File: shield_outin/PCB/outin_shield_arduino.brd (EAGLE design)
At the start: 68.6 x 53.3 mm, 27 parts, among them SW1 POWER, SW2 I2C_PWR, SW3 SERIAL_PWR, SW4 SWITCH-TACT-6MM

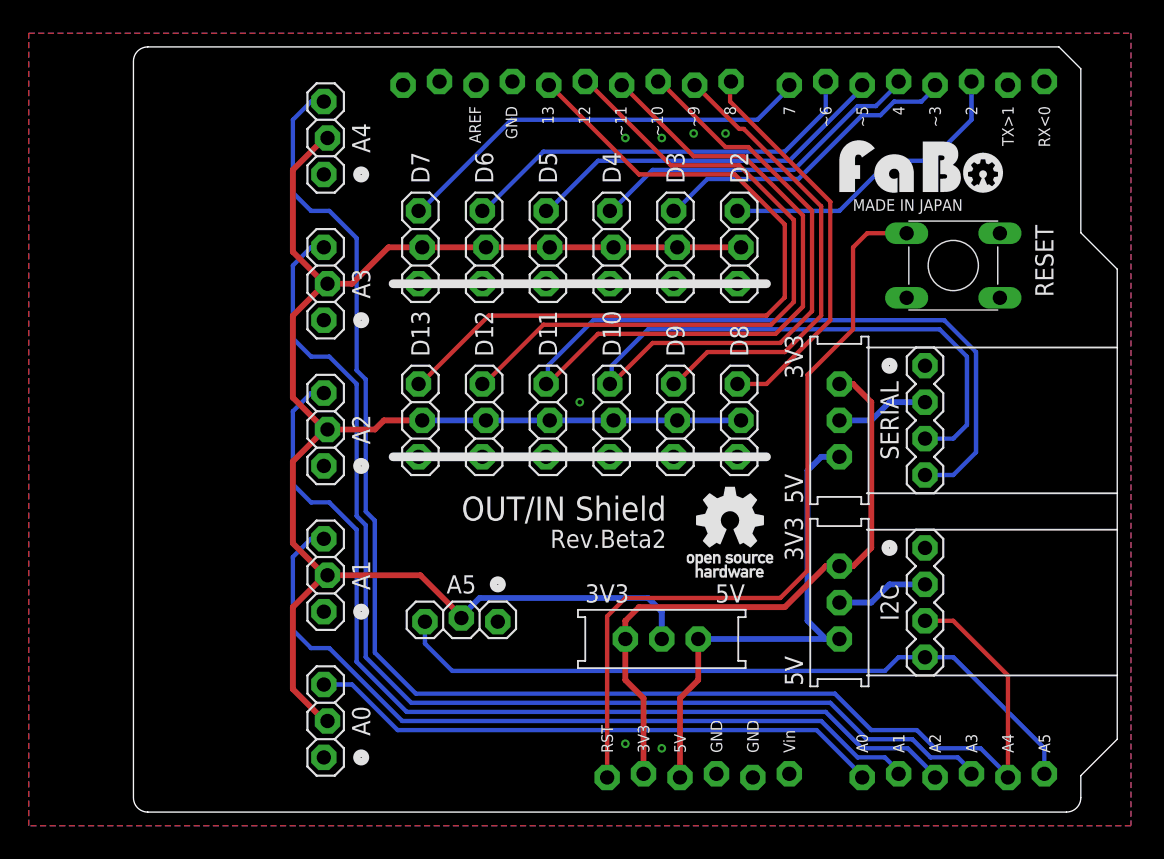
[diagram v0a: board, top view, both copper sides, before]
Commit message: change serial vcc level convert  outin_shield_arduino
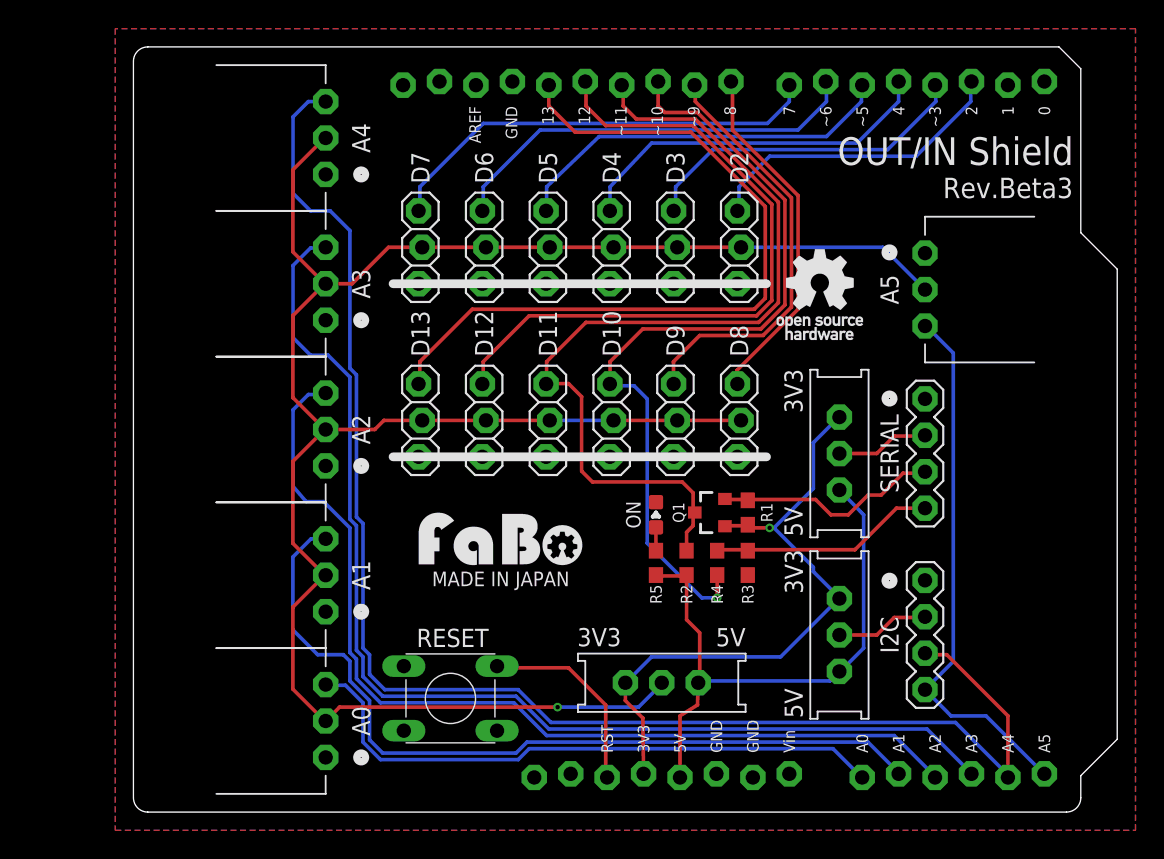
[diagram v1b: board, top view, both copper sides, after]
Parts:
- added ON: (no value), Gclue:EIA0603-LED
- added Q1: (no value), Gclue:SOT23-3
- added R1, R2, R3, R4, R5: (no value), Gclue:EIA0603
- A0, A1, A2, A3, A4, A5: device Gclue:1X3-SNEAKY -> Gclue:BRICK_3PIN_CONNECTOR
- SW4: value SWITCH-TACT-6MM -> RESET
- moved SW4 46.3 mm to (22.1, 7.92)
- moved A5 39.7 mm to (55.2, 36.4), turned to 270 degrees
- moved U$5 39.2 mm to (25.6, 17.2)
- moved U$4 17.7 mm to (47.9, 36.9)
- moved SW1 3.05 mm to (36.8, 9.02)
- moved SV2 2.31 mm to (55.2, 25.0)
- moved SW3 2.31 mm to (49.2, 25.0)
- moved SV1 2.26 mm to (55.2, 12.3)
- moved SW2 2.26 mm to (49.2, 12.3)
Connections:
- removed net RESET: SW4.4, U1.RESET
- new net N$2: SW4.3, U1.RESET
- new net N$4: ON.A, R5.2
- new net RX: R3.2, R4.1, SV2.RX
- new net TX: Q1.2, R1.1, SV2.TX
- net 3V3: now also Q1.1, R1.2
- net 5V: now also R2.2, R5.1
- net GND: now also A0.GND, A1.GND, A2.GND, A3.GND, A4.GND, A5.GND, ON.C, R3.1, SW4.2; no longer A0.1, A1.1, A2.1, A3.1, A4.1, A5.1, SW4.1
- net OUT10: now also R4.2; no longer SV2.RX
- net OUT11: now also Q1.3, R2.1; no longer SV2.TX
- net SEN0: now also A0.IN/OUT; no longer A0.3
- net SEN1: now also A1.IN/OUT; no longer A1.3
- net SEN2: now also A2.IN/OUT; no longer A2.3
- net SEN3: now also A3.IN/OUT; no longer A3.3
- net SEN4: now also A4.IN/OUT; no longer A4.3
- net SEN5: now also A5.IN/OUT; no longer A5.3
- net VCC: now also A0.VCC, A1.VCC, A2.VCC, A3.VCC, A4.VCC, A5.VCC; no longer A0.2, A1.2, A2.2, A3.2, A4.2, A5.2
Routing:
- net RESET: track 54.5 -> 0.00 mm
- net OUT11: track 87.5 -> 62.2 mm
- net OUT10: track 73.6 -> 57.1 mm, vias 0 -> 1
- net RX: track 0.00 -> 15.8 mm
- net TX: track 0.00 -> 15.7 mm
- net N$2: track 0.00 -> 13.8 mm
- net SEN5: track 50.3 -> 37.8 mm
- net VCC: track 135.5 -> 146.2 mm, vias 0 -> 1
- net 5V: track 34.9 -> 41.7 mm
- net SEN1: track 54.3 -> 57.4 mm
- net OUT8: track 27.9 -> 24.8 mm
- net OUT9: track 32.2 -> 29.6 mm
- net SEN0: track 40.3 -> 42.3 mm
- net OUT4: track 23.9 -> 25.7 mm
- net N$4: track 0.00 -> 1.63 mm
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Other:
- board text added: "0"
- board text added: "1"
- board text added: "Rev.Beta3"
- board text removed: "RX<0"
- board text removed: "Rev.Beta2"
- board text removed: "TX>1"

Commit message: change layout outin_shield_arduino
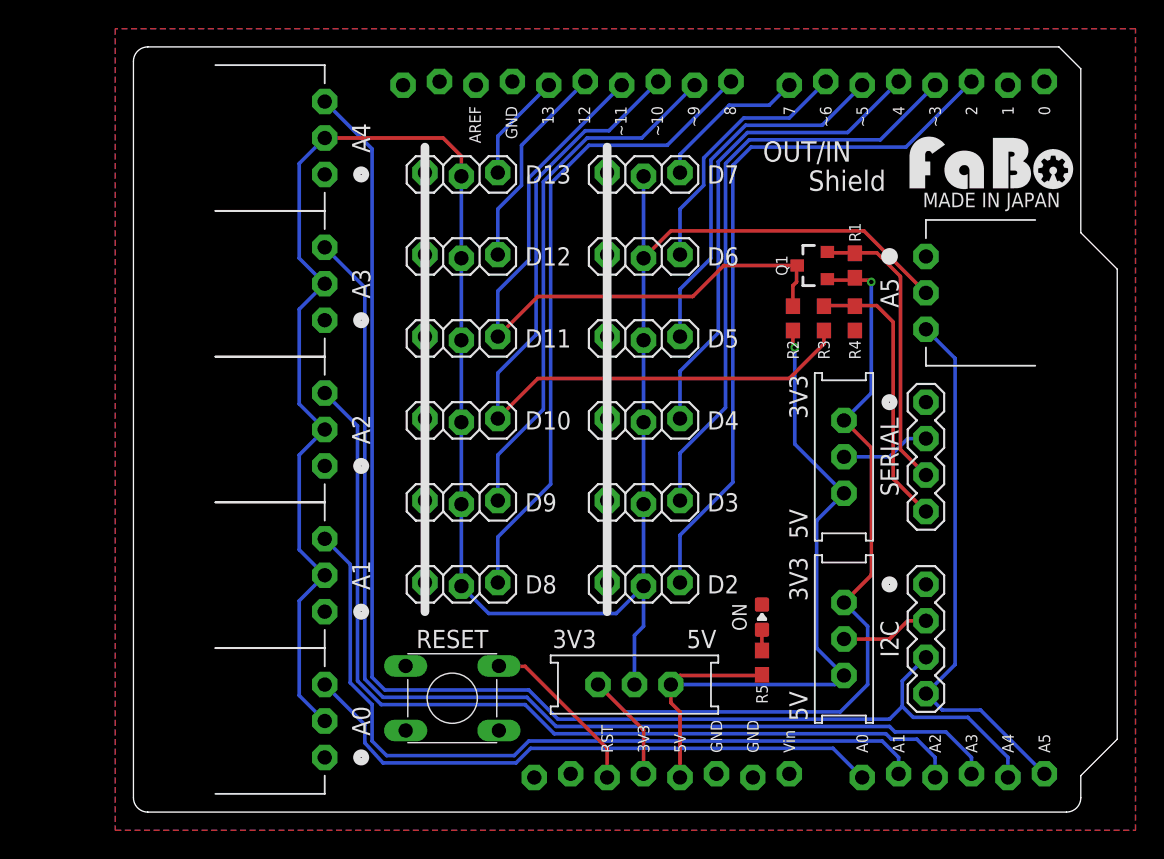
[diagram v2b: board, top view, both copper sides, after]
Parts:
- removed U$4: (no value), Gclue:LOGO_OSHW_T_M
- added U$2: (no value), Gclue:LOGO_OSHW_T_M_BOTTOM
- OUT10, OUT11, OUT12, OUT13, OUT2, OUT3, OUT4, OUT5, OUT6, OUT7, OUT8, OUT9: device Gclue:1X3-SNEAKY -> Gclue:1X3-SNEAKY-BRICK
- moved U$5 43.1 mm to (59.8, 43.4)
- moved OUT2 24.4 mm to (35.6, 15.9), turned to 0 degrees
- moved OUT8 22.5 mm to (22.9, 15.9), turned to 0 degrees
- moved R4 19.6 mm to (50.3, 34.4), turned to 90 degrees
- moved R1 18.8 mm to (50.3, 38.1)
- moved Q1 18.6 mm to (47.4, 38.1)
- moved R2 18.6 mm to (46.0, 34.4)
- moved OUT3 17.9 mm to (35.6, 21.6), turned to 0 degrees
- moved R3 17.9 mm to (48.1, 34.4), turned to 270 degrees
- moved OUT13 17.4 mm to (22.9, 44.5), turned to 0 degrees
- moved OUT7 16.4 mm to (35.6, 44.5), turned to 0 degrees
- moved OUT9 16.0 mm to (22.9, 21.6), turned to 0 degrees
- moved OUT4 12.3 mm to (35.6, 27.3), turned to 0 degrees
- moved OUT12 11.5 mm to (22.9, 38.7), turned to 0 degrees
- moved OUT6 11.1 mm to (35.6, 38.7), turned to 0 degrees
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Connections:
- net GND: now also R4.1; no longer R3.1
- net OUT10: now also R3.2; no longer R4.2
- net RX: now also R3.1, R4.2; no longer R3.2, R4.1
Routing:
- net OUT13: track 53.3 -> 7.57 mm
- net OUT12: track 47.7 -> 14.6 mm
- net OUT2: track 21.7 -> 49.7 mm
- net OUT7: track 31.1 -> 10.9 mm
- net OUT8: track 24.8 -> 44.9 mm
- net 3V3: track 44.3 -> 62.5 mm
- net OUT3: track 23.5 -> 41.7 mm
- net OUT11: track 62.2 -> 47.0 mm
- net VCC: track 146.2 -> 158.8 mm, vias 1 -> 0
- net OUT6: track 29.5 -> 18.1 mm
- net 5V: track 41.7 -> 52.8 mm, vias 0 -> 1
- net SEN4: track 104.1 -> 94.4 mm
- net OUT4: track 25.7 -> 33.9 mm
- net OUT9: track 29.6 -> 36.9 mm
- net TX: track 15.7 -> 20.4 mm
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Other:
- board text added: "OUT/IN"
- board text added: "Shield"
- board text removed: "OUT/IN Shield"

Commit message: add brick_i2c_proximity
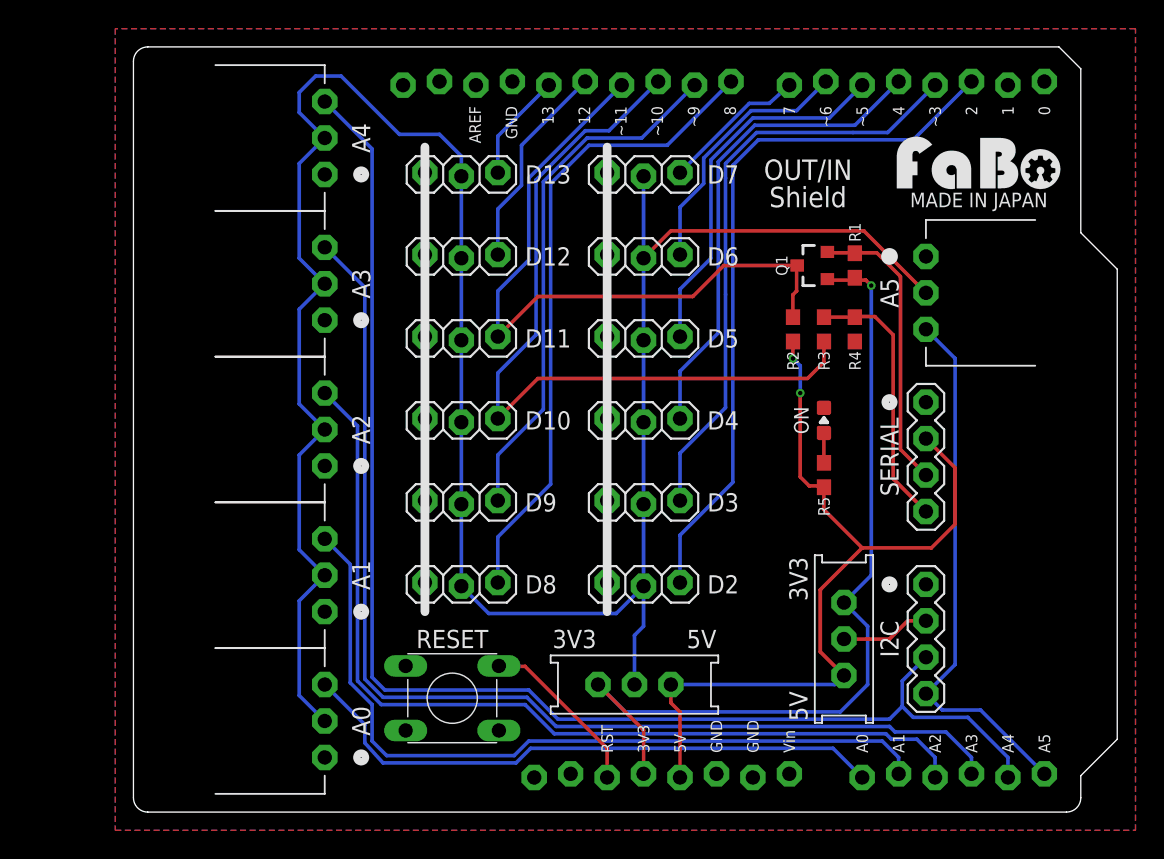
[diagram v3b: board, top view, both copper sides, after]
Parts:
- removed SV1: (no value), Gclue:BRICK_I2C_CONNECTOR
- removed SV2: (no value), Gclue:BRICK_SERIAL_CONNECTOR
- removed SW3: SERIAL_PWR, Gclue:EG1218
- added I2C_CON: (no value), FaBo-Template:FABO_BRICK_I2C_CONNECTOR
- added SERIAL_CON: (no value), FaBo-Template:FABO_BRICK_SERIAL_CONNECTOR
- R1, R2: value (none) -> 10k
- R3: value (none) -> 3k
- R4: value (none) -> 4k7
- R5: value (none) -> 220
- U1: device Gclue:ARDUINO_UNO_R3_OUTIN -> FaBo-Boards:ARDUINO_UNO_R3_NOLABEL
- moved ON 14.4 mm to (48.1, 27.3)
- moved R5 13.8 mm to (48.1, 23.5)
- moved U$2 2.29 mm to (63.0, 26.7), turned to 90 degrees
- moved U$5 0.89 mm to (58.9, 43.4)
- moved R2 0.76 mm to (46.0, 33.7)
- moved R3 0.76 mm to (48.1, 33.7)
- moved R4 0.76 mm to (50.3, 33.7)
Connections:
- removed net SERIAL_PWR: SV2.VCC, SW3.2
- net 3V3: no longer SW3.3
- net 5V: now also SERIAL_CON.VCC; no longer SW3.1
- net GND: now also I2C_CON.GND, SERIAL_CON.GND; no longer SV1.GND, SV2.GND
- net I2C_PWR: now also I2C_CON.VCC; no longer SV1.VCC
- net RX: now also SERIAL_CON.RX; no longer SV2.RX
- net SEN4: now also I2C_CON.SDA; no longer SV1.SDA
- net SEN5: now also I2C_CON.SCL; no longer SV1.SCL
- net TX: now also SERIAL_CON.TX; no longer SV2.TX
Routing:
- net 5V: track 52.8 -> 60.8 mm, vias 1 -> 2
- net VCC: track 158.8 -> 166.7 mm
- net SERIAL_PWR: track 6.24 -> 0.00 mm
- net 3V3: track 62.5 -> 60.8 mm
- net RX: track 19.5 -> 18.6 mm
- net OUT7: track 10.9 -> 10.1 mm
- net OUT11: track 47.0 -> 47.7 mm
- net N$4: track 1.45 -> 2.08 mm
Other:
- board text added: "Rev.Beta4"
- board text removed: "Rev.Beta3"

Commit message: change Revision
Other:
- board text added: "Rev.1.0.0"
- board text removed: "Rev.Beta4"
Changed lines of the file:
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@@
 <text x="22.225" y="12.065" size="1.27" layer="21" font="vector" ratio="12" rot="R180" align="center">RESET</text>
 <text x="53.34" y="12.065" size="1.27" layer="21" font="vector" ratio="12" rot="R270" align="top-center">I2C</text>
-<text x="65.0621" y="1.27" size="1.016" layer="22" font="vector" ratio="12" rot="MR180" align="bottom-right">Rev.Beta4</text>
+<text x="65.0621" y="1.27" size="1.016" layer="22" font="vector" ratio="12" rot="MR180" align="bottom-right">Rev.1.0.0</text>
 <text x="44.323" y="42.164" size="1.4224" layer="21" font="vector" ratio="12">Shield</text>
 <text x="53.34" y="24.765" size="1.27" layer="21" font="vector" ratio="12" rot="R270" align="top-center">SERIAL</text>
